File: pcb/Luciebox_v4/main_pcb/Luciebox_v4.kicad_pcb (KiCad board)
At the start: 2 copper layers, 100 x 100 mm, 77 parts, among them J1 USB_B_Mini, P1 Power, P2 Analog, P3 Digital, P4 Digital, P5 CONN_01X01, P6 CONN_01X01, P7 CONN_01X01, P8 CONN_01X01, Q1 N-Channel_Mosfet, SW1 Switch_tilt, SW2 Switch_tilt, SW3 Switch_tilt, SW4 Switch_tilt, T1 terminal_3x1, T10 terminal_8x1, T11 terminal_8x1, T12 terminal_8x1, T13 terminal_8x1, T2 terminal_3x1, T3 terminal_3x1, T4 terminal_3x1, T5 terminal_8x1, T6 terminal_8x1, T7 terminal_3x1, T8 terminal_3x1, T9 terminal_3x1, U1 CA56-12SRWA, U2 8X8PADS, U3 ATmega328-PU, Y1 16MHz

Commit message: V4 main pcb ready for layouting
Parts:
- removed G***: LOGO, artwork:lines_burst
- removed G***: LOGO, artwork:wallpaper_abstract
- removed P1: Power, Socket_Arduino_Uno:Socket_Strip_Arduino_1x08
- removed P2: Analog, Socket_Arduino_Uno:Socket_Strip_Arduino_1x06
- removed P3: Digital, Socket_Arduino_Uno:Socket_Strip_Arduino_1x10
- removed P4: Digital, Socket_Arduino_Uno:Socket_Strip_Arduino_1x08
- removed P5, P7, P8: CONN_01X01, Socket_Arduino_Uno:Arduino_1pin
- removed R14: 10K, Luciebox:1206_0805
- removed R24: R_Small, Luciebox:1206_0805
- removed R_0_if_no_touch1: 0, Luciebox:1206_0805
- removed S2: selector_knob, Luciebox:Rotary_Switch
- removed SW1, SW2, SW3, SW4: Switch_tilt, Luciebox:Terminal_2x1_100mil
- removed T10, T11, T12, T13: terminal_8x1, Luciebox:Terminal_8x1_100mil
- removed T3, T9: terminal_3x1, Luciebox:Terminal_3x1_100mil
- added A1: Arduino_UNO_R3, Module:Arduino_UNO_R3, B.Cu at (36.3, 63.1)
- added D10: D_Schottky, Luciebox:D_SMA, F.Cu at (31.0, 69.0)
- added D2: D_Schottky, Luciebox:D_SMA, F.Cu at (38.0, 69.2)
- added D3: D_Schottky, Luciebox:D_SMA, F.Cu at (40.5, 69.2)
- added D4: D_Schottky, Luciebox:D_SMA, F.Cu at (43.2, 69.2)
- added D5: D_Schottky, Luciebox:D_SMA, F.Cu at (46.0, 69.2)
- added D6: D_Schottky, Luciebox:D_SMA, F.Cu at (48.8, 69.2)
- added D7: D_Schottky, Luciebox:D_SMA, F.Cu at (51.8, 69.2)
- added D8: D_Schottky, Luciebox:D_SMA, F.Cu at (54.0, 69.2)
- added D9: D_Schottky, Luciebox:D_SMA, F.Cu at (33.2, 69.0)
- added Q2: NPN transistor, Luciebox:SOT-23, F.Cu at (54.8, 6.00)
- added R26: 1K, Luciebox:0603_1608Metric, F.Cu at (56.8, 2.32)
- added R27: 10K, Luciebox:0603_1608Metric, F.Cu at (57.8, 6.82)
- added R28: 100K, Luciebox:0603_1608Metric, F.Cu at (59.3, 6.75)
- added R_0_if_no_auto_power_off1: 0, Luciebox:0603_1608Metric, F.Cu at (43.5, 5.75)
- C1, C2, C3: footprint Luciebox:0805 -> Luciebox:0603_1608Metric
- D1: footprint Luciebox:smd_throughhole_2_pins -> Luciebox:D_SMA
- P6: value CONN_01X01 -> Power
- Q1: value N-Channel_Mosfet -> P-Channel MOSFET; footprint Luciebox:TO-220-3 -> Package_TO_SOT_SMD:SOT-23
- R1, R2, R3, R4, R5: value 10K -> 100; footprint Luciebox:1206_0805 -> Luciebox:0603_1608Metric
- R10: value 100K -> R_Small; footprint Luciebox:1206_0805 -> Luciebox:0603_1608Metric
- R11, R12, R13, R6, R7, R8, R9: value 10K -> R_Small; footprint Luciebox:1206_0805 -> Luciebox:0603_1608Metric
- R15, R16, R17, R18: value 100 -> R_Small; footprint Luciebox:1206_0805 -> Luciebox:0603_1608Metric
- R19: value 100 -> 1M; footprint Luciebox:1206_0805 -> Luciebox:0603_1608Metric
- R20: value 1M -> R_Small; footprint Luciebox:1206_0805 -> Luciebox:0603_1608Metric
- R21: value DAC_R-2R -> R_Small; footprint Luciebox:SIP-10 -> Luciebox:0603_1608Metric
- R22, R23, R_0_if_no_usb_switch1, R_reset_pullup1, R_vcc_protected1: footprint Luciebox:1206_0805 -> Luciebox:0603_1608Metric
- R25: value R_Small -> 100K; footprint Luciebox:1206_0805 -> Luciebox:0603_1608Metric
- T1, T4: value terminal_3x1 -> terminal_8x1; footprint Luciebox:Terminal_3x1_100mil -> Luciebox:Terminal_8x1_100mil
- T5: value terminal_8x1 -> terminal_3x1; footprint Luciebox:Terminal_8x1_100mil -> Luciebox:Terminal_3x1_100mil
- T7, T8: value terminal_3x1 -> terminal_8x1; footprint Luciebox:Terminal_3x1_100mil -> Luciebox:Terminal_8x1_100mil; moved to F.Cu
- moved H3 206.6 mm to (49.5, 205.7)
- moved H4 204.5 mm to (26.7, 207.6)
- moved H6 155.0 mm to (49.5, 213.4)
- moved H8 152.1 mm to (51.4, 221.0)
- moved H5 149.7 mm to (26.7, 213.4)
- moved P6 148.6 mm to (3.84, -129.2)
- moved H7 127.4 mm to (28.6, 221.0)
- moved H2 112.6 mm to (49.5, 198.1)
- moved H1 103.3 mm to (26.7, 196.2)
- moved D1 75.9 mm to (35.8, 69.2)
- moved R10 71.2 mm to (75.8, 49.8), turned to 90 degrees
- moved R9 68.0 mm to (71.2, 53.5), turned to -90 degrees
- moved T2 60.0 mm to (74.5, 70.2), turned to -90 degrees
- moved R5 59.7 mm to (42.0, 20.3), turned to 90 degrees
- moved R4 57.3 mm to (43.5, 20.3), turned to 90 degrees
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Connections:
- D1 pad 1: Net-(D1-Pad1) -> /7
- J1 pad 5: Net-(D1-Pad2) -> Net-(D9-Pad2)
- P6 pad 1: unconnected-(P6-Pad1) -> (no net)
- Q1 pad 2: GND -> /Vin
- Q1 pad 3: Net-(Q1-Pad3) -> VCC
- R1 pad 2: GND -> /6(PWM)
- R10 pad 1: Net-(Q1-Pad1) -> /A2
- R10 pad 2: Net-(Q1-Pad3) -> Net-(R10-Pad2)
- R11 pad 1: Net-(R11-Pad1) -> Net-(R10-Pad2)
- R12 pad 1: Net-(R12-Pad1) -> Net-(R11-Pad2)
- R12 pad 2: Net-(R11-Pad1) -> Net-(R12-Pad2)
- R13 pad 1: Net-(R13-Pad1) -> Net-(R12-Pad2)
- R13 pad 2: Net-(R12-Pad1) -> GND
- R15 pad 1: Net-(R15-Pad1) -> /A1
- R15 pad 2: /6(PWM) -> Net-(R15-Pad2)
- R16 pad 2: /5(PWM) -> Net-(R16-Pad2)
- R17 pad 2: /9(PWM) -> Net-(R17-Pad2)
- R18 pad 2: /10(PWM-SS) -> Net-(R18-Pad2)
- R19 pad 1: Net-(R19-Pad1) -> Net-(C2-Pad2)
- R19 pad 2: /11(PWM-MOSI) -> Net-(C3-Pad2)
- R2 pad 2: Net-(R1-Pad1) -> /5(PWM)
- R20 pad 1: Net-(C2-Pad2) -> /A1
- R20 pad 2: Net-(C3-Pad2) -> Net-(R16-Pad1)
- R21 pad 1: (no net) -> Net-(R16-Pad1)
- R21 pad 2: (no net) -> Net-(R17-Pad1)
- R22 pad 1: (no net) -> Net-(R17-Pad1)
- R22 pad 2: (no net) -> Net-(R18-Pad1)
- R23 pad 1: (no net) -> Net-(R18-Pad1)
- R23 pad 2: (no net) -> GND
- R25 pad 1: (no net) -> /Vin
- R25 pad 2: (no net) -> Net-(Q1-Pad1)
- R3 pad 2: Net-(R2-Pad1) -> /9(PWM)
- R4 pad 2: Net-(R3-Pad1) -> /10(PWM-SS)
- R5 pad 2: Net-(R4-Pad1) -> /11(PWM-MOSI)
- R6 pad 1: Net-(R6-Pad1) -> /A2
- R6 pad 2: Net-(R5-Pad1) -> Net-(R6-Pad2)
- R7 pad 1: Net-(R7-Pad1) -> Net-(R10-Pad2)
- R7 pad 2: Net-(R6-Pad1) -> Net-(R7-Pad2)
- R8 pad 2: Net-(R7-Pad1) -> Net-(R8-Pad2)
- R9 pad 1: /A4(SDA) -> Net-(R12-Pad2)
- R9 pad 2: Net-(Q1-Pad1) -> Net-(R9-Pad2)
- R_0_if_no_usb_switch1 pad 1: Net-(D1-Pad1) -> Net-(D9-Pad1)
- R_0_if_no_usb_switch1 pad 2: VCC -> /Vin
- T1 pad 1: /2 -> Net-(D1-Pad2)
- T1 pad 2: /3(PWM) -> Net-(D2-Pad2)
- T1 pad 3: GND -> Net-(D3-Pad2)
- T2 pad 1: /A0 -> /2
- T2 pad 2: VCC_minimalCurrent -> /3(PWM)
- T2 pad 3: GND -> /A5(SCL)
- T4 pad 1: /A0 -> Net-(R18-Pad2)
- T4 pad 2: VCC_minimalCurrent -> Net-(R17-Pad2)
- T4 pad 3: GND -> Net-(R16-Pad2)
- T5 pad 1: GND -> Net-(J1-Pad2)
- T5 pad 2: VCC_minimalCurrent -> Net-(J1-Pad4)
- T5 pad 3: /A1 -> Net-(J1-Pad3)
- T6 pad 2: VCC_minimalCurrent -> VCC
- T6 pad 3: /A2 -> Net-(R1-Pad1)
- T6 pad 4: Net-(R15-Pad1) -> GND
- T6 pad 5: /A3 -> Net-(D10-Pad2)
- T6 pad 6: /1(Tx) -> /A0
- T6 pad 7: /4 -> Net-(R26-Pad2)
- T6 pad 8: /13(SCK) -> unconnected-(T6-Pad8)
- T7 pad 1: Net-(R19-Pad1) -> unconnected-(T7-Pad1)
- T7 pad 2: /7 -> unconnected-(T7-Pad2)
- T7 pad 3: /13(SCK) -> unconnected-(T7-Pad3)
- T8 pad 1: Net-(R18-Pad1) -> /Vin
- T8 pad 2: Net-(R17-Pad1) -> Net-(D9-Pad1)
- T8 pad 3: /A3 -> Net-(D10-Pad2)
- U1 pad 12: Net-(R19-Pad1) -> Net-(R5-Pad1)
- U1 pad 6: Net-(R16-Pad1) -> Net-(R2-Pad1)
- U1 pad 8: Net-(R17-Pad1) -> Net-(R3-Pad1)
- U1 pad 9: Net-(R18-Pad1) -> Net-(R4-Pad1)
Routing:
- net GND: track 436.5 -> 0.00 mm, vias 7 -> 0
- net VCC: track 178.7 -> 0.00 mm, vias 3 -> 0
- net /0(Rx): track 150.7 -> 0.00 mm, vias 4 -> 0
- net VCC_minimalCurrent: track 142.1 -> 0.00 mm
- net /A3: track 137.1 -> 0.00 mm, vias 2 -> 0
- net /1(Tx): track 136.1 -> 0.00 mm, vias 3 -> 0
- net /7: track 132.7 -> 0.00 mm, vias 4 -> 0
- net /A4(SDA): track 127.7 -> 0.00 mm, vias 4 -> 0
- net /A5(SCL): track 126.1 -> 0.00 mm, vias 4 -> 0
- net /8: track 124.2 -> 0.00 mm, vias 6 -> 0
- net /A0: track 112.8 -> 0.00 mm, vias 1 -> 0
- net Net-(R_reset_pullup1-Pad2): track 101.7 -> 0.00 mm, vias 3 -> 0
- net /A1: track 95.2 -> 0.00 mm, vias 1 -> 0
- net (no net): track 94.4 -> 0.00 mm, vias 1 -> 0
- net /3(PWM): track 93.3 -> 0.00 mm, vias 2 -> 0
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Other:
- board size 100 x 100 mm -> 355 x 241.4 mm
- board text added: "1 Settings 2 Stopwatch 3 MultiTimer 4 School 5 Pomodoro 6 Gamble 7 Score 8 Simon 9 Reaction 10 Wackamole 11 Guitarhero"
- board text added: "1 Settings 2 Stopwatch 3 MultiTimer 4 School 5 Pomodoro 6 Gamble 7 Score 8 Simon 9 Reaction 10 Wackamole 11 Guitarhero 12 Drawing 13 Memory 14 Music 15 Movie 16 Metronome 17 Sequencer 18 Notes 19 Composer 20 Noise 21 Hacker 22 Baby"
- board text added: "12 Drawing 13 Memory 14 Music 15 Movie 16 Metronome 17 Sequencer 18 Notes 19 Composer 20 Noise 21 Hacker 22 Baby"
- board text added: "Luciebox v4.0 a nonkel Lode production 2020-12 luciebox.ameije.com"
- board text added: "ON: B1 OFF: B1 + B5 APP SELECT: B1 + B8 APP RESET: B1 + B6"
- board text removed: "1"
- board text removed: "Luciebox v3.0 a nonkel Lode production 2020-12 luciebox.ameije.com"

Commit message: layout main board start
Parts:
- moved H6 208.2 mm to (42.2, 5.25)
- moved H4 168.8 mm to (-38.1, 51.8)
- moved H5 168.8 mm to (-38.1, 57.5)
- moved H7 168.8 mm to (-36.2, 65.1)
- moved H8 168.8 mm to (-13.3, 65.1)
- moved H1 144.1 mm to (42.8, 53.0)
- moved H3 124.8 mm to (72.0, 83.0)
- moved H2 123.6 mm to (5.75, 82.5)
- moved R2 15.6 mm to (33.5, 11.7)
- moved R3 15.6 mm to (32.0, 11.8)
- moved R4 15.6 mm to (30.5, 11.8)
- moved R5 15.6 mm to (29.0, 11.8)
- moved A1 2.14 mm to (34.3, 62.4)
- moved D10 1.25 mm to (29.8, 69.0)
- moved D1 0.25 mm to (35.8, 69.0)
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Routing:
- removed copper zone on F.Cu, net GND
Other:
- board size 355 x 241.4 mm -> 78 x 100 mm
- board text added: "12 Drawing 13 Memory 14 Music 15 Media 16 Metronome 17 Sequencer 18 Notes 19 Composer 20 Noise 21 Hacker 22 Baby"
- board text added: "Applications 1 Settings 2 Stopwatch 3 MultiTimer 4 School 5 Pomodoro 6 Gamble 7 Score 8 Simon 9 Reaction 10 Wackamole 11 Guitarhero"
- board text added: "Luciebox v4.0 a nonkel Lode production 2022-05 luciebox.ameije.com"
- board text removed: "1 Settings 2 Stopwatch 3 MultiTimer 4 School 5 Pomodoro 6 Gamble 7 Score 8 Simon 9 Reaction 10 Wackamole 11 Guitarhero"
- board text removed: "1 Settings 2 Stopwatch 3 MultiTimer 4 School 5 Pomodoro 6 Gamble 7 Score 8 Simon 9 Reaction 10 Wackamole 11 Guitarhero 12 Drawing 13 Memory 14 Music 15 Movie 16 Metronome 17 Sequencer 18 Notes 19 Composer 20 Noise 21 Hacker 22 Baby"
- board text removed: "12 Drawing 13 Memory 14 Music 15 Movie 16 Metronome 17 Sequencer 18 Notes 19 Composer 20 Noise 21 Hacker 22 Baby"
- board text removed: "AUX Power Supply"
- board text removed: "BAT +"
- board text removed: "BAT -"
- board text removed: "DAC_A0"
- board text removed: "DAC_A1"
- board text removed: "DAC_A2"
- board text removed: "DAC_A4"
- board text removed: "GND"
- board text removed: "Luciebox v4.0 a nonkel Lode production 2020-12 luciebox.ameije.com"
- board text removed: "ON-Switch"
- board text removed: "RX"
- board text removed: "Reset"
- board text removed: "TX"
- board text removed: "Touch Power ON"
- board text removed: "VCC"

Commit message: Pcb v4 evolution
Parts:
- removed P6: Power, Socket_Arduino_Uno:Arduino_1pin
- A1: footprint Module:Arduino_UNO_R3 -> Module:Arduino_UNO_R3_WithMountingHoles; moved to F.Cu
- BZ1, S1, T1, T4, T6, T7, T8, U1, U3, Y1: moved to B.Cu
- moved R10 72.3 mm to (3.50, 52.7)
- moved R6 72.3 mm to (3.50, 56.2)
- moved R11 69.3 mm to (5.00, 52.7)
- moved R7 69.3 mm to (5.00, 56.2)
- moved R12 66.6 mm to (6.50, 52.7)
- moved R8 66.3 mm to (6.50, 56.2)
- moved BZ1 65.0 mm to (6.50, 22.5)
- moved R9 63.3 mm to (8.00, 56.2)
- moved R13 63.3 mm to (8.00, 52.7)
- moved R20 59.6 mm to (9.50, 52.7)
- moved R15 59.6 mm to (9.50, 56.2)
- moved H1 58.3 mm to (95.0, 27.2)
- moved R21 56.6 mm to (11.0, 52.7)
- moved R16 56.6 mm to (11.0, 56.2)
- moved T4 54.6 mm to (10.8, 75.5), turned to 180 degrees
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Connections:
- Q2 pad 2: Net-(Q2-Pad2) -> Net-(R27-Pad1)
- R26 pad 1: Net-(Q2-Pad2) -> Net-(R27-Pad1)
- R27 pad 1: /A4 -> Net-(R27-Pad1)
- R27 pad 2: Net-(Q2-Pad2) -> /A4
- R28 pad 2: /A4 -> Net-(R27-Pad1)
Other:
- board size 78 x 100 mm -> 427 x 288 mm

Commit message: Progress on pcb's
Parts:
- moved J1 96.1 mm to (0.21, 94.2), turned to 0 degrees
- moved T5 80.1 mm to (12.0, 95.0), turned to 90 degrees
- moved U2 40.8 mm to (53.7, 88.8)
- moved R_vcc_protected1 39.8 mm to (58.3, 4.98)
- moved H1 25.7 mm to (71.9, 16.0)
- moved D10 24.5 mm to (45.8, 69.8), turned to -90 degrees
- moved D8 24.0 mm to (21.5, 69.8), turned to -90 degrees
- moved T2 23.8 mm to (75.0, 94.0)
- moved H6 20.5 mm to (4.83, 16.0)
- moved D7 19.5 mm to (23.8, 69.8), turned to -90 degrees
- moved D9 17.5 mm to (42.2, 69.8), turned to -90 degrees
- moved D6 13.5 mm to (26.8, 69.8), turned to -90 degrees
- moved D1 12.5 mm to (39.8, 69.8), turned to -90 degrees
- moved D2 8.00 mm to (37.5, 69.8), turned to -90 degrees
- moved D5 8.00 mm to (29.5, 69.8), turned to -90 degrees
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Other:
- board size 427 x 288 mm -> 220 x 150 mm

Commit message: Delete Arduino Uno footprint. Line up bottonboard and main pcb
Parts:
- removed A1: Arduino_UNO_R3, Module:Arduino_UNO_R3_WithMountingHoles
- removed H4, H5, H7, H8: MountingHole, Luciebox:MountingHole_4.3mm_M4
- added J2: USB_B_Mini, Luciebox:usb_mini_Molex-0548190519, F.Cu at (77.9, 94.8)
- U2: footprint Luciebox:64_PADS_100mil -> Luciebox:8X8PADS_100mil
- moved R10 57.2 mm to (54.4, 78.8)
- moved R11 57.2 mm to (55.9, 78.8)
- moved R12 57.2 mm to (57.4, 78.8)
- moved R13 57.2 mm to (58.9, 78.8)
- moved R15 57.2 mm to (60.4, 82.3)
- moved R16 57.2 mm to (61.9, 82.3)
- moved R17 57.2 mm to (63.4, 82.3)
- moved R20 57.2 mm to (60.4, 78.8)
- moved R21 57.2 mm to (61.9, 78.8)
- moved R22 57.2 mm to (63.4, 78.8)
- moved R6 57.2 mm to (54.4, 82.3)
- moved R7 57.2 mm to (55.9, 82.3)
- moved R8 57.2 mm to (57.4, 82.3)
- moved R9 57.2 mm to (58.9, 82.3)
- moved R18 57.2 mm to (64.9, 82.3)
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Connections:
- U2 pad 11: Net-(U2-Pad10) -> Net-(U2-Pad11)
- U2 pad 12: Net-(U2-Pad10) -> Net-(U2-Pad11)
- U2 pad 15: Net-(U2-Pad15) -> Net-(U2-Pad13)
- U2 pad 16: Net-(U2-Pad15) -> Net-(U2-Pad13)
- U2 pad 19: Net-(U2-Pad17) -> Net-(U2-Pad19)
- U2 pad 20: Net-(U2-Pad17) -> Net-(U2-Pad19)
- U2 pad 23: Net-(U2-Pad23) -> Net-(U2-Pad21)
- U2 pad 24: Net-(U2-Pad23) -> Net-(U2-Pad21)
- U2 pad 25: Net-(U2-Pad25) -> unconnected-(U2-Pad25)
- U2 pad 26: Net-(U2-Pad25) -> unconnected-(U2-Pad26)
- U2 pad 27: Net-(U2-Pad25) -> unconnected-(U2-Pad27)
- U2 pad 28: Net-(U2-Pad25) -> unconnected-(U2-Pad28)
- U2 pad 29: Net-(U2-Pad29) -> unconnected-(U2-Pad29)
- U2 pad 30: Net-(U2-Pad29) -> Net-(U2-Pad30)
- U2 pad 31: Net-(U2-Pad31) -> Net-(U2-Pad30)
- U2 pad 32: Net-(U2-Pad31) -> Net-(U2-Pad30)
- U2 pad 33: Net-(U2-Pad33) -> unconnected-(U2-Pad33)
- U2 pad 34: Net-(U2-Pad33) -> unconnected-(U2-Pad34)
- U2 pad 35: Net-(U2-Pad33) -> unconnected-(U2-Pad35)
- U2 pad 36: Net-(U2-Pad33) -> unconnected-(U2-Pad36)
- U2 pad 37: Net-(U2-Pad37) -> unconnected-(U2-Pad37)
- U2 pad 38: Net-(U2-Pad37) -> Net-(U2-Pad38)
- U2 pad 39: Net-(U2-Pad39) -> Net-(U2-Pad38)
- U2 pad 40: Net-(U2-Pad39) -> Net-(U2-Pad38)
- U2 pad 41: Net-(U2-Pad41) -> unconnected-(U2-Pad41)
- U2 pad 42: Net-(U2-Pad41) -> unconnected-(U2-Pad42)
- U2 pad 43: Net-(U2-Pad41) -> unconnected-(U2-Pad43)
- U2 pad 44: Net-(U2-Pad41) -> unconnected-(U2-Pad44)
- U2 pad 45: Net-(U2-Pad45) -> unconnected-(U2-Pad45)
- U2 pad 46: Net-(U2-Pad45) -> Net-(U2-Pad46)
- U2 pad 47: Net-(U2-Pad47) -> Net-(U2-Pad46)
- U2 pad 48: Net-(U2-Pad47) -> Net-(U2-Pad46)
- U2 pad 49: Net-(U2-Pad49) -> unconnected-(U2-Pad49)
- U2 pad 50: Net-(U2-Pad49) -> unconnected-(U2-Pad50)
- U2 pad 51: Net-(U2-Pad49) -> unconnected-(U2-Pad51)
- U2 pad 52: Net-(U2-Pad49) -> unconnected-(U2-Pad52)
- U2 pad 53: Net-(U2-Pad53) -> unconnected-(U2-Pad53)
- U2 pad 54: Net-(U2-Pad53) -> Net-(U2-Pad54)
- U2 pad 55: Net-(U2-Pad55) -> Net-(U2-Pad54)
- U2 pad 56: Net-(U2-Pad55) -> Net-(U2-Pad54)
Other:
- board size 220 x 150 mm -> 78 x 100 mm
- board text added: "Applications 1 Settings 2 Stopwatch 3 MultiTimer 4 School 5 Pomodoro 6 Random 7 Score 8 Simon 9 Reaction 10 Wackamole 11 Guitar Hero"
- board text removed: "Applications 1 Settings 2 Stopwatch 3 MultiTimer 4 School 5 Pomodoro 6 Gamble 7 Score 8 Simon 9 Reaction 10 Wackamole 11 Guitarhero"

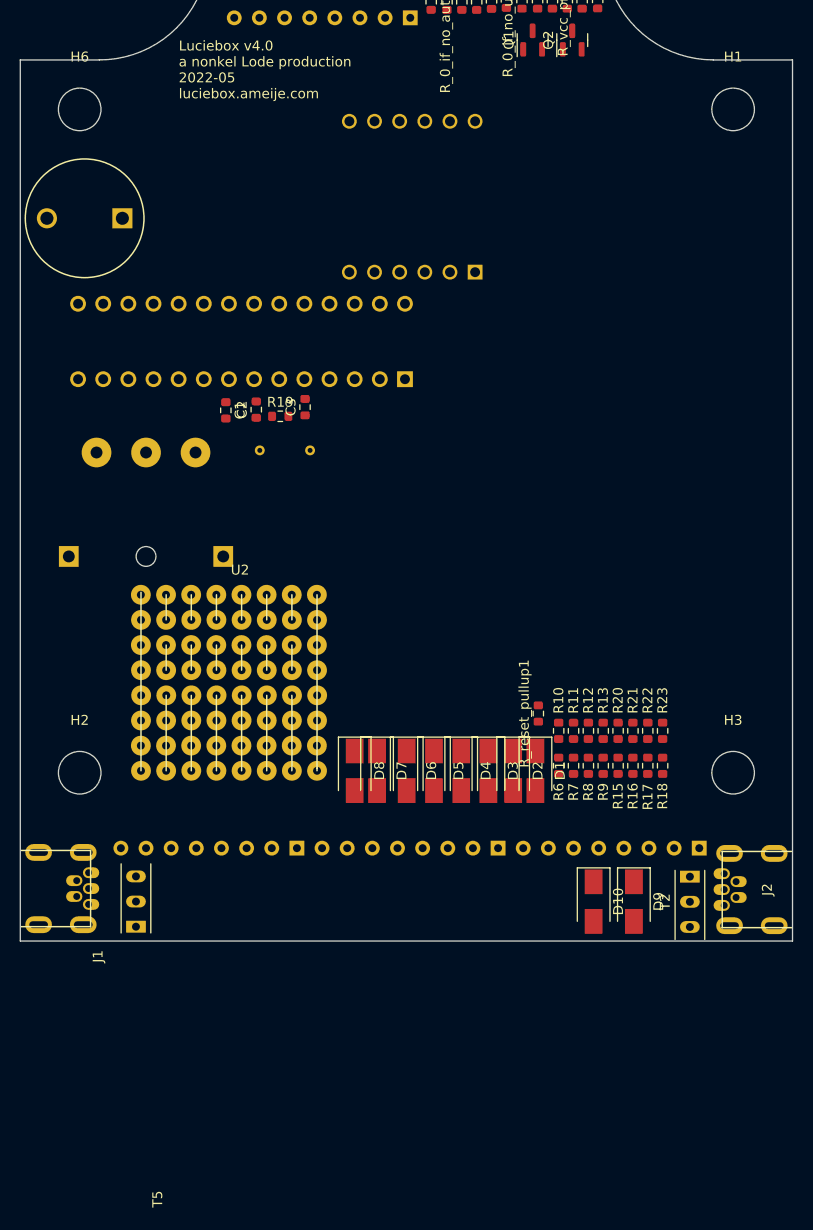
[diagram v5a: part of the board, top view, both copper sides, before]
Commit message: Main board pcb prevent interference with buttons from button board
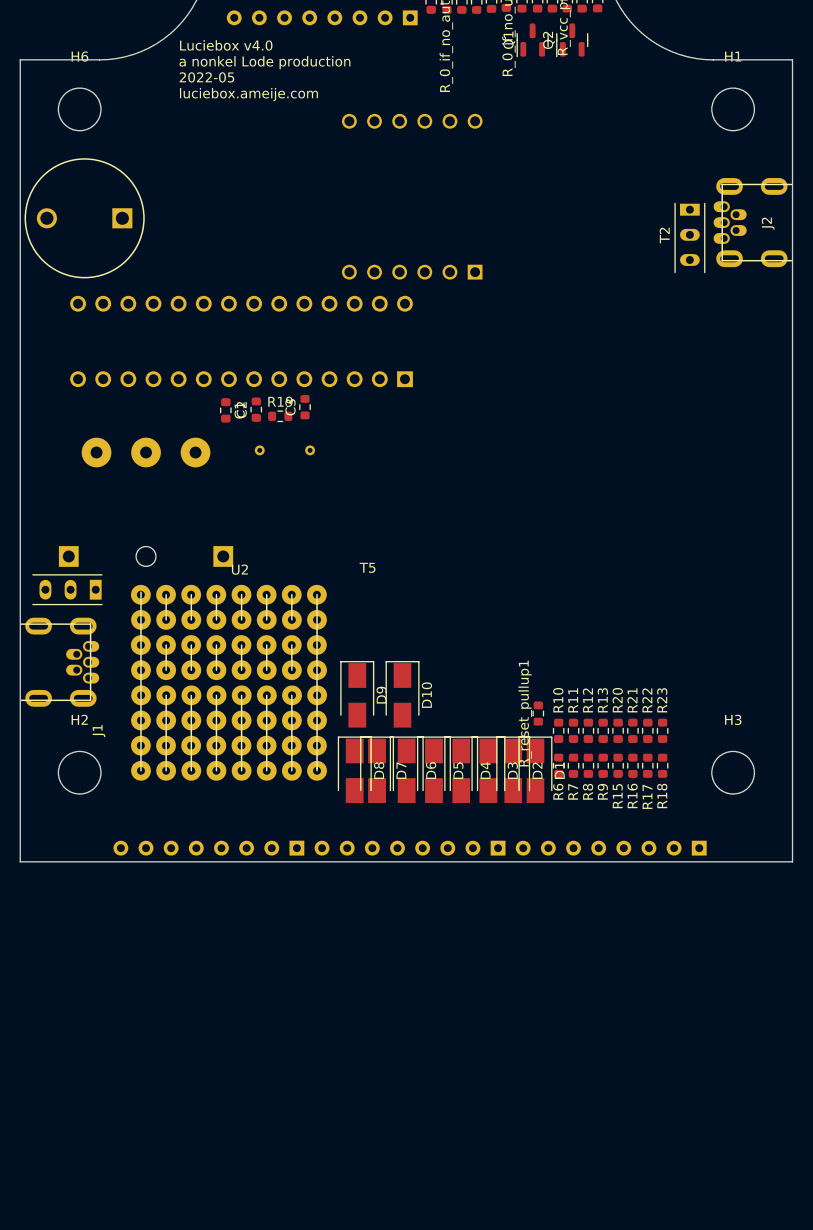
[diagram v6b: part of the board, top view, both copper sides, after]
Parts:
- moved J2 67.4 mm to (77.9, 27.4)
- moved T2 67.4 mm to (67.6, 28.7)
- moved D9 34.8 mm to (34.0, 75.2)
- moved T5 32.2 mm to (5.08, 64.5), turned to 180 degrees
- moved D10 28.4 mm to (38.6, 75.2)
- moved J1 22.9 mm to (0.10, 71.8)
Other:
- board size 78 x 100 mm -> 78 x 92 mm
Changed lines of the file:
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@@
   )
   (footprint "Luciebox:Terminal_3x1_100mil" (layer "F.Cu")
-    (at 11.684 96.012 90)
+    (at 5.08 64.516 180)
     (property "Sheetfile" "Luciebox_v4.kicad_sch")
     (property "Sheetname" "")
     (attr through_hole)
-    (fp_text reference "T5" (at -30.055 2.185 90) (layer "F.SilkS")
-      (effects (font (size 1 1) (thickness 0.15)))
-    )
-    (fp_text value "terminal_3x1" (at 0 -2.5 90) (layer "F.Fab")
+    (fp_text reference "T5" (at -30.055 2.185) (layer "F.SilkS")
+      (effects (font (size 1 1) (thickness 0.15)))
+    )
+    (fp_text value "terminal_3x1" (at 0 -2.5) (layer "F.Fab")
       (effects (font (size 1 1) (thickness 0.15)))
     )
@@
     (fp_line (start -5.93 -1.27) (end 3.81 -1.27) (layer "F.CrtYd") (width 0.05))
     (fp_line (start -3.39 1.25) (end -3.39 -1.25) (layer "F.CrtYd") (width 0.05))
-    (pad "1" thru_hole rect (at -2.54 0 90) (size 1.2 2) (drill 0.8) (layers *.Cu *.Mask)
+    (pad "1" thru_hole rect (at -2.54 0 180) (size 1.2 2) (drill 0.8) (layers *.Cu *.Mask)
       (net 7 "Net-(J1-Pad2)") (pinfunction "1") (pintype "input"))
-    (pad "2" thru_hole oval (at 0 0 90) (size 1.2 2) (drill 0.8) (layers *.Cu *.Mask)
+    (pad "2" thru_hole oval (at 0 0 180) (size 1.2 2) (drill 0.8) (layers *.Cu *.Mask)
       (net 9 "Net-(J1-Pad4)") (pinfunction "2") (pintype "input"))
-    (pad "3" thru_hole oval (at 2.54 0 90) (size 1.2 2) (drill 0.8) (layers *.Cu *.Mask)
+    (pad "3" thru_hole oval (at 2.54 0 180) (size 1.2 2) (drill 0.8) (layers *.Cu *.Mask)
       (net 8 "Net-(J1-Pad3)") (pinfunction "3") (pintype "input"))
   )
@@
   )
   (footprint "Luciebox:D_SMA" (layer "F.Cu")
-    (at 57.912 96.012 -90)
+    (at 38.608 75.184 -90)
     (descr "Diode SMA (DO-214AC)")
     (tags "Diode SMA (DO-214AC)")
@@
   )
   (footprint "Luciebox:D_SMA" (layer "F.Cu")
-    (at 61.976 96.012 -90)
+    (at 34.036 75.184 -90)
     (descr "Diode SMA (DO-214AC)")
     (tags "Diode SMA (DO-214AC)")
@@
   )
   (footprint "Luciebox:usb_mini_Molex-0548190519" (layer "F.Cu")
-    (at 0.1 94.7)
+    (at 0.1 71.84)
     (property "Sheetfile" "Luciebox_v4.kicad_sch")
     (property "Sheetname" "")
@@
   )
   (footprint "Luciebox:usb_mini_Molex-0548190519" (layer "F.Cu")
-    (at 77.9 94.8 180)
+    (at 77.9 27.432 180)
     (property "Sheetfile" "Luciebox_v4.kicad_sch")
     (property "Sheetname" "")
@@
   )
   (footprint "Luciebox:Terminal_3x1_100mil" (layer "F.Cu")
-    (at 67.634 96.0385 -90)
+    (at 67.634 28.6705 -90)
     (property "Sheetfile" "Luciebox_v4.kicad_sch")
     (property "Sheetname" "")
@@
   (gr_line (start 29.972 65.024) (end 29.972 82.55) (layer "F.SilkS") (width 0.15))
   (gr_line (start 24.892 82.804) (end 24.892 75.184) (layer "F.SilkS") (width 0.15))
-  (gr_line (start 78 100) (end 0 100) (layer "Edge.Cuts") (width 0.1))
+  (gr_line (start 78 92) (end 0 92) (layer "Edge.Cuts") (width 0.1))
   (gr_line (start 0 11) (end 8 11) (layer "Edge.Cuts") (width 0.1))
   (gr_arc (start 70 11) (mid 62.221825 7.778175) (end 59 0) (layer "Edge.Cuts") (width 0.1))
-  (gr_line (start 0 100) (end 0 11) (layer "Edge.Cuts") (width 0.1))
+  (gr_line (start 0 92) (end 0 11) (layer "Edge.Cuts") (width 0.1))
   (gr_line (start 59 0) (end 19 0) (layer "Edge.Cuts") (width 0.1))
-  (gr_line (start 78 11) (end 78 100) (layer "Edge.Cuts") (width 0.1))
+  (gr_line (start 78 11) (end 78 92) (layer "Edge.Cuts") (width 0.1))
   (gr_arc (start 18.999999 0) (mid 15.778174 7.778175) (end 7.999999 11) (layer "Edge.Cuts") (width 0.1))
   (gr_line (start 70 11) (end 78 11) (layer "Edge.Cuts") (width 0.1))
